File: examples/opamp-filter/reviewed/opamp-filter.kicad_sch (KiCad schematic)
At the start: 19 parts, among them J1 IN, J2 5V, J3 OUT, U1 MCP6001R, U2 MCP6001R

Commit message: Route the sheets, and anchor the ground vias where the loop is
The user's verdict on the last round stood: none of the five schematics
read as a human drawing, and the artwork still had its physics wrong.
This round answers both.

The schematic side replaces the stub-and-label sheet with a router.
Every signal net becomes a tree of straight, L-, Z- and detour-shaped
runs on the 1.27 mm grid: legs leave a pin along its own stub, escape
distances stagger so a bus does not fight over one column, every pin
reserves a runway another wire may cross but not ride along, and the
sheet frame, title block and notes are obstacles like any symbol.
Fragments merge Kruskal-style so a rail whose regulator is boxed in
still gets its capacitors chained; each surviving fragment keeps one
label, because the label is what names the net. Collinear same-net
segments are unioned and then split at every tee - KiCad 9's
connectivity requires files drawn the way the editor draws them, with
a junction dot and a wire break wherever a branch tees in, and a wire
that runs through a junction connects on one side of it only. That
last fact cost an evening and is now a comment.

Trying to draw the wires found what no rule had: the buck's LED was
upside down with its ground pointing up into the resistor above it,
both breakout headers faced away from everything they connect to
(fixed with mirrored symbols, which Part now supports), the FPGA
sheet's notes printed over the 1.2 V regulator, and its programming
header sat inside the title block. Wired: buck, motor and op-amp
completely; the Pico carrier 31 of 33 nets; the FPGA board 16 of 19 -
what stays labelled is what a human would label too.

The artwork side anchors every FPGA decoupling capacitor's ground via
against its own pad, on the far side from the supply pad, with the
1.2 mm stub as the whole loop - retiring all seven
layout.decoupling_via findings and that waiver with them. A back_cost
experiment (0.4 to 0.6) to shrink the return-path cuts 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
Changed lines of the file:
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@@
   	(comment 2 "from tools/make_examples.py in sabas0ba/kicad_skills")
   )
-  (wire (pts (xy 38.1 100.33) (xy 48.26 100.33)) (stroke (width 0) (type default)))
+  (wire (pts (xy 38.1 100.33) (xy 44.45 100.33)) (stroke (width 0) (type default)))
+  (wire (pts (xy 44.45 100.33) (xy 48.26 100.33)) (stroke (width 0) (type default)))
+  (wire (pts (xy 44.45 100.33) (xy 44.45 113.03)) (stroke (width 0) (type default)))
+  (wire (pts (xy 60.96 100.33) (xy 69.85 100.33)) (stroke (width 0) (type default)))
+  (wire (pts (xy 69.85 100.33) (xy 78.74 100.33)) (stroke (width 0) (type default)))
+  (wire (pts (xy 69.85 100.33) (xy 69.85 123.19)) (stroke (width 0) (type default)))
+  (wire (pts (xy 121.92 100.33) (xy 129.54 100.33)) (stroke (width 0) (type default)))
+  (wire (pts (xy 129.54 100.33) (xy 146.05 100.33)) (stroke (width 0) (type default)))
+  (wire (pts (xy 146.05 97.79) (xy 146.05 100.33)) (stroke (width 0) (type default)))
+  (wire (pts (xy 129.54 100.33) (xy 129.54 123.19)) (stroke (width 0) (type default)))
+  (wire (pts (xy 91.44 100.33) (xy 109.22 100.33)) (stroke (width 0) (type default)))
+  (wire (pts (xy 109.22 63.5) (xy 109.22 100.33)) (stroke (width 0) (type default)))
+  (wire (pts (xy 100.33 63.5) (xy 109.22 63.5)) (stroke (width 0) (type default)))
+  (wire (pts (xy 201.93 100.33) (xy 217.17 100.33)) (stroke (width 0) (type default)))
+  (wire (pts (xy 217.17 100.33) (xy 217.17 133.35)) (stroke (width 0) (type default)))
+  (wire (pts (xy 217.17 133.35) (xy 224.79 133.35)) (stroke (width 0) (type default)))
   (wire (pts (xy 74.93 171.45) (xy 74.93 184.15)) (stroke (width 0) (type default)))
+  (wire (pts (xy 105.41 173.99) (xy 135.89 173.99)) (stroke (width 0) (type default)))
+  (wire (pts (xy 135.89 172.72) (xy 135.89 173.99)) (stroke (width 0) (type default)))
+  (wire (pts (xy 74.93 171.45) (xy 105.41 171.45)) (stroke (width 0) (type default)))
+  (wire (pts (xy 105.41 171.45) (xy 105.41 173.99)) (stroke (width 0) (type default)))
   (wire (pts (xy 173.99 100.33) (xy 189.23 100.33)) (stroke (width 0) (type default)))
-  (wire (pts (xy 201.93 100.33) (xy 217.17 100.33)) (stroke (width 0) (type default)))
-  (wire (pts (xy 60.96 100.33) (xy 78.74 100.33)) (stroke (width 0) (type default)))
-  (wire (pts (xy 91.44 100.33) (xy 109.22 100.33)) (stroke (width 0) (type default)))
+  (wire (pts (xy 173.99 100.33) (xy 173.99 110.49)) (stroke (width 0) (type default)))
+  (wire (pts (xy 146.05 110.49) (xy 173.99 110.49)) (stroke (width 0) (type default)))
+  (wire (pts (xy 146.05 102.87) (xy 146.05 110.49)) (stroke (width 0) (type default)))
+  (wire (pts (xy 100.33 102.87) (xy 146.05 102.87)) (stroke (width 0) (type default)))
+  (wire (pts (xy 100.33 76.2) (xy 100.33 102.87)) (stroke (width 0) (type default)))
+  (wire (pts (xy 129.54 177.8) (xy 134.62 177.8)) (stroke (width 0) (type default)))
+  (wire (pts (xy 134.62 177.8) (xy 135.89 177.8)) (stroke (width 0) (type default)))
+  (wire (pts (xy 129.54 135.89) (xy 129.54 177.8)) (stroke (width 0) (type default)))
+  (wire (pts (xy 69.85 135.89) (xy 129.54 135.89)) (stroke (width 0) (type default)))
+  (wire (pts (xy 163.83 165.1) (xy 163.83 175.26)) (stroke (width 0) (type default)))
+  (wire (pts (xy 134.62 165.1) (xy 163.83 165.1)) (stroke (width 0) (type default)))
+  (wire (pts (xy 134.62 165.1) (xy 134.62 177.8)) (stroke (width 0) (type default)))
+  (junction (at 44.45 100.33) (diameter 0) (color 0 0 0 0))
+  (junction (at 69.85 100.33) (diameter 0) (color 0 0 0 0))
+  (junction (at 74.93 171.45) (diameter 0) (color 0 0 0 0))
+  (junction (at 105.41 173.99) (diameter 0) (color 0 0 0 0))
+  (junction (at 109.22 100.33) (diameter 0) (color 0 0 0 0))
+  (junction (at 129.54 100.33) (diameter 0) (color 0 0 0 0))
+  (junction (at 129.54 135.89) (diameter 0) (color 0 0 0 0))
+  (junction (at 134.62 177.8) (diameter 0) (color 0 0 0 0))
+  (junction (at 146.05 102.87) (diameter 0) (color 0 0 0 0))
+  (junction (at 173.99 100.33) (diameter 0) (color 0 0 0 0))
+  (junction (at 217.17 100.33) (diameter 0) (color 0 0 0 0))
   (wire (pts (xy 35.56 100.33) (xy 38.1 100.33)) (stroke (width 0) (type default)))
   (label "IN" (at 38.1 100.33 0) (effects (font (size 1.27 1.27)) (justify left bottom)))
@@
   )
   (wire (pts (xy 69.85 125.73) (xy 69.85 123.19)) (stroke (width 0) (type default)))
-  (label "IN_DC" (at 69.85 123.19 0) (effects (font (size 1.27 1.27)) (justify left bottom)))
   (wire (pts (xy 69.85 133.35) (xy 69.85 135.89)) (stroke (width 0) (type default)))
-  (label "VREF" (at 69.85 135.89 0) (effects (font (size 1.27 1.27)) (justify left bottom)))
   (symbol (lib_id "Device:R") (at 69.85 129.54 0.0) (unit 1)
     (exclude_from_sim no) (in_bom yes) (on_board yes) (dnp no)
@@
   )
   (wire (pts (xy 100.33 66.04) (xy 100.33 63.5)) (stroke (width 0) (type default)))
-  (label "X" (at 100.33 63.5 0) (effects (font (size 1.27 1.27)) (justify left bottom)))
   (wire (pts (xy 100.33 73.66) (xy 100.33 76.2)) (stroke (width 0) (type default)))
-  (label "OUT" (at 100.33 76.2 0) (effects (font (size 1.27 1.27)) (justify left bottom)))
   (symbol (lib_id "Device:C") (at 100.33 69.85 0.0) (unit 1)
     (exclude_from_sim no) (in_bom yes) (on_board yes) (dnp no)
@@
   )
   (wire (pts (xy 129.54 125.73) (xy 129.54 123.19)) (stroke (width 0) (type default)))
-  (label "FILT_IN" (at 129.54 123.19 0) (effects (font (size 1.27 1.27)) (justify left bottom)))
   (wire (pts (xy 129.54 133.35) (xy 129.54 135.89)) (stroke (width 0) (type default)))
-  (label "VREF" (at 129.54 135.89 0) (effects (font (size 1.27 1.27)) (justify left bottom)))
   (symbol (lib_id "Device:C") (at 129.54 129.54 0.0) (unit 1)
     (exclude_from_sim no) (in_bom yes) (on_board yes) (dnp no)
@@
   )
   (wire (pts (xy 152.4 97.79) (xy 146.05 97.79)) (stroke (width 0) (type default)))
-  (label "FILT_IN" (at 146.05 97.79 0) (effects (font (size 1.27 1.27)) (justify left bottom)))
   (wire (pts (xy 152.4 102.87) (xy 146.05 102.87)) (stroke (width 0) (type default)))
-  (label "OUT" (at 146.05 102.87 0) (effects (font (size 1.27 1.27)) (justify left bottom)))
   (wire (pts (xy 157.48 92.71) (xy 157.48 86.36)) (stroke (width 0) (type default)))
   (symbol (lib_id "power:+5V") (at 157.48 86.36 180) (unit 1)
@@
   )
   (wire (pts (xy 105.41 176.53) (xy 105.41 173.99)) (stroke (width 0) (type default)))
-  (label "MID" (at 105.41 173.99 0) (effects (font (size 1.27 1.27)) (justify left bottom)))
   (wire (pts (xy 105.41 184.15) (xy 105.41 186.69)) (stroke (width 0) (type default)))
   (symbol (lib_id "power:GND") (at 105.41 186.69 0) (unit 1)
@@
   )
   (wire (pts (xy 142.24 172.72) (xy 135.89 172.72)) (stroke (width 0) (type default)))
-  (label "MID" (at 135.89 172.72 0) (effects (font (size 1.27 1.27)) (justify left bottom)))
   (wire (pts (xy 142.24 177.8) (xy 135.89 177.8)) (stroke (width 0) (type default)))
-  (label "VREF" (at 135.89 177.8 0) (effects (font (size 1.27 1.27)) (justify left bottom)))
   (wire (pts (xy 147.32 167.64) (xy 147.32 161.29)) (stroke (width 0) (type default)))
   (symbol (lib_id "power:+5V") (at 147.32 161.29 180) (unit 1)
@@
   )
   (wire (pts (xy 44.45 115.57) (xy 44.45 113.03)) (stroke (width 0) (type default)))
-  (label "IN" (at 44.45 113.03 0) (effects (font (size 1.27 1.27)) (justify left bottom)))
   (wire (pts (xy 44.45 123.19) (xy 44.45 125.73)) (stroke (width 0) (type default)))
   (symbol (lib_id "power:GND") (at 44.45 125.73 0) (unit 1)
@@
   )
   (wire (pts (xy 224.79 135.89) (xy 224.79 133.35)) (stroke (width 0) (type default)))
-  (label "OUT_AC" (at 224.79 133.35 0) (effects (font (size 1.27 1.27)) (justify left bottom)))
   (wire (pts (xy 224.79 143.51) (xy 224.79 146.05)) (stroke (width 0) (type default)))
   (symbol (lib_id "power:GND") (at 224.79 146.05 0) (unit 1)

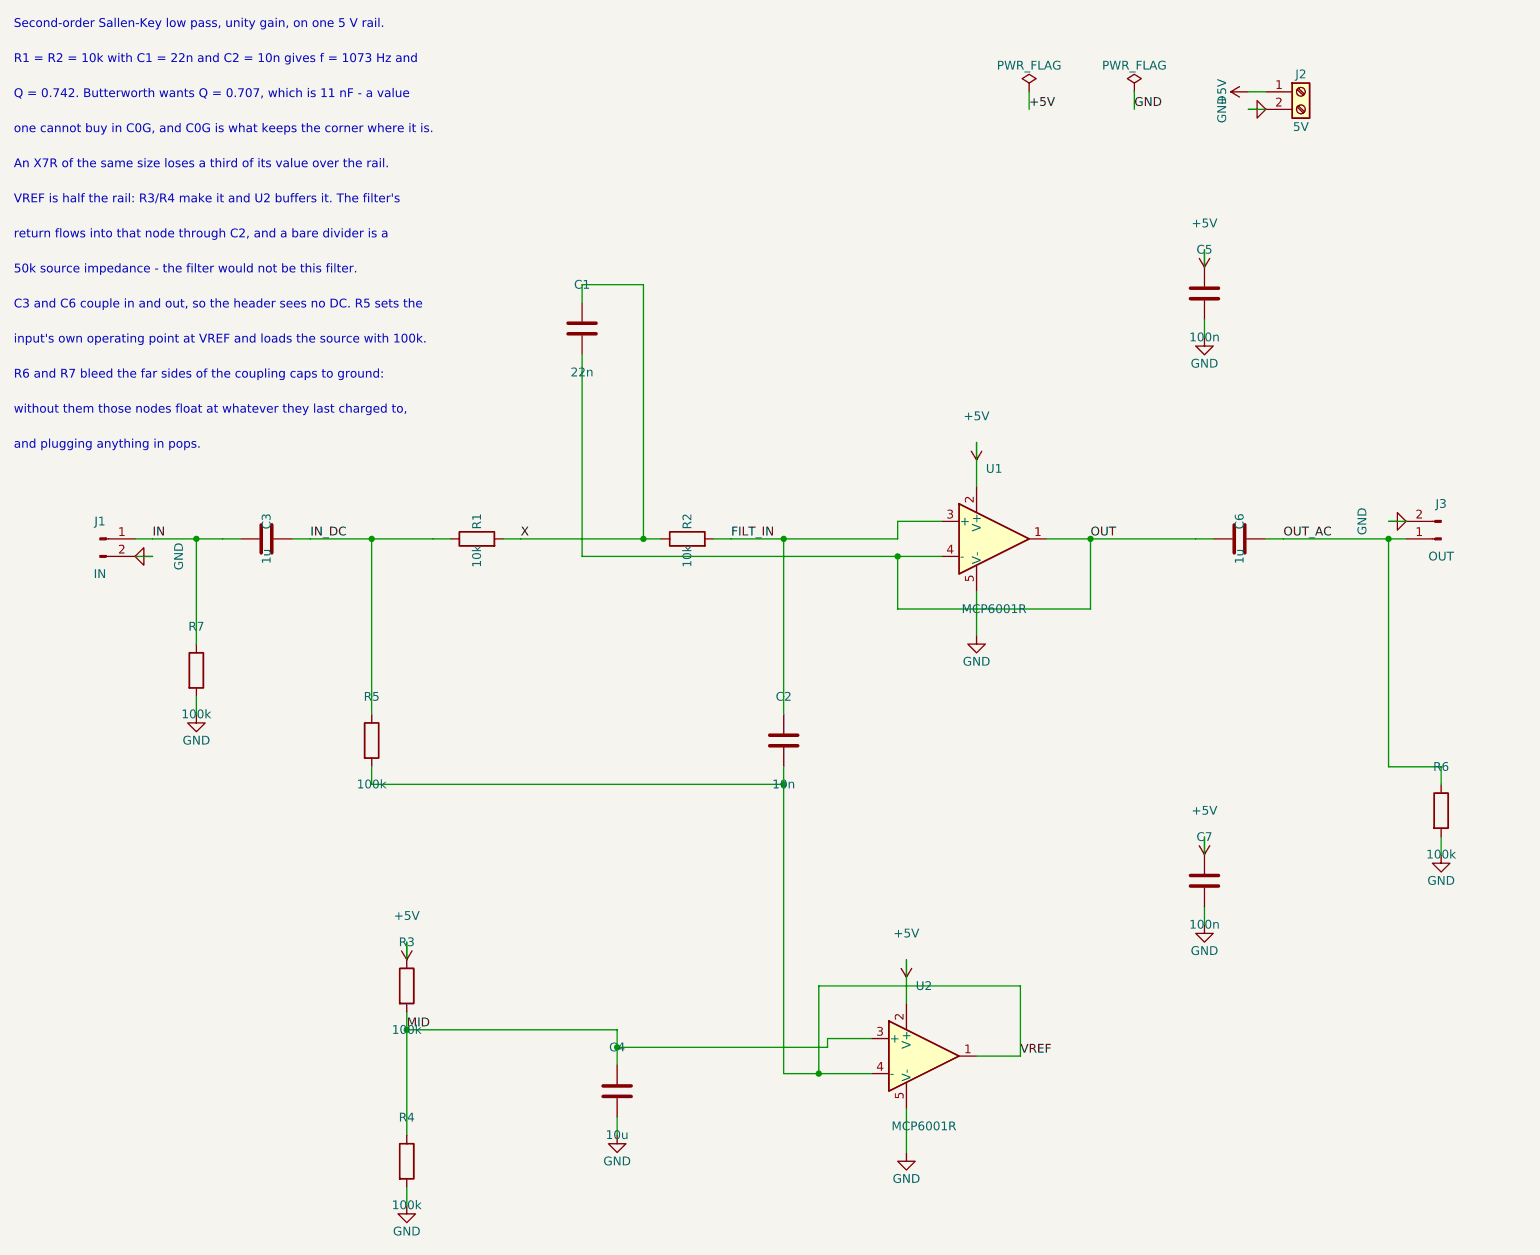
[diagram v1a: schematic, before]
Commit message: Regenerate the five with stitched pours, silk that speaks, and wires that never double back
All ten variants rebuilt by the fixed generator: reviewed boards carry
ground on both faces with the stitching ring (buck 35 vias, fpga 116),
thru_hole_only front pours, the board id and connector pin names in
silk, and the buck's explicit ground return; the sheets hook power up
through upright symbols and source-anchored flags with no overlapping
wires and no junction-less tees left. Every reviewed variant passes its
own gate with zero errors; every as-generated variant still fails, now
also for the rules this round added.

Co-Authored-By: Claude Fable 5 <noreply@anthropic.com>
Claude-Session: https://claude.ai/code/session_01DUj7Ltu92tWg159mCSacwY
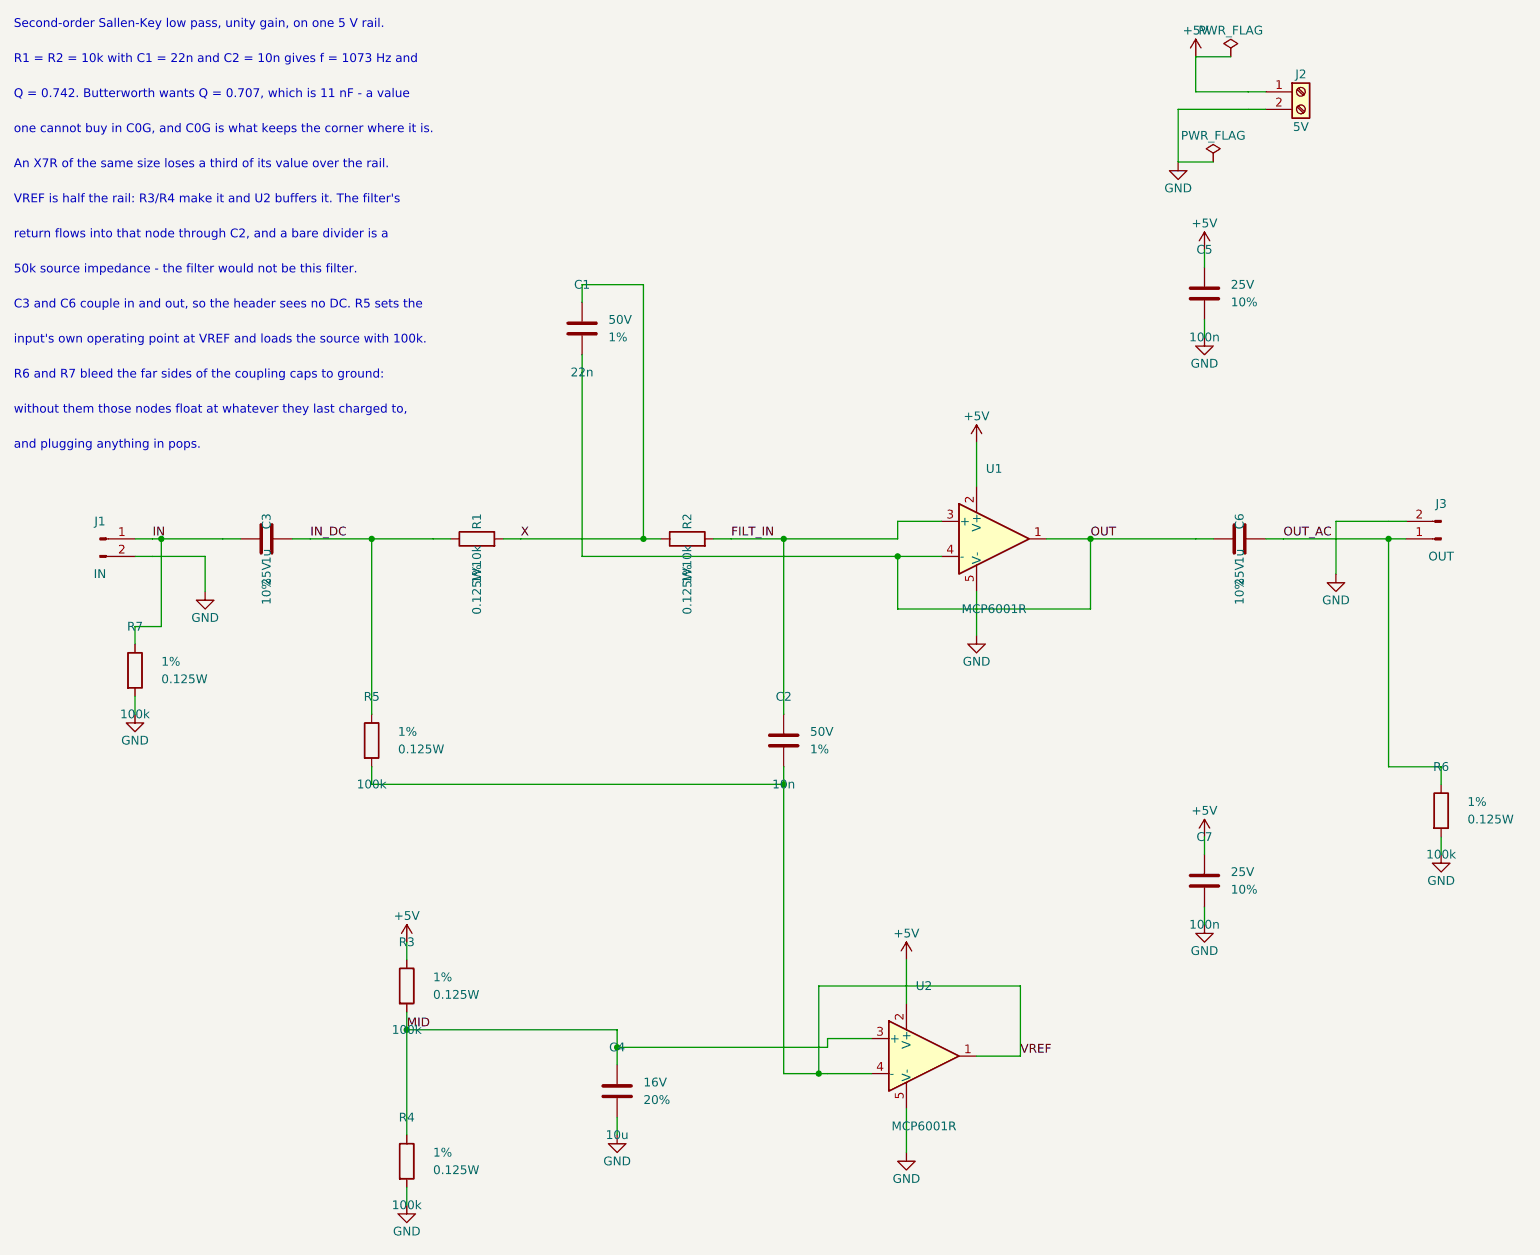
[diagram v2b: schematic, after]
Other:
- moved on the sheet: R7
